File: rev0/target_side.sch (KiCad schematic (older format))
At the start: 11 parts, among them IC1 ECP5-BGA256, U9 USB3343

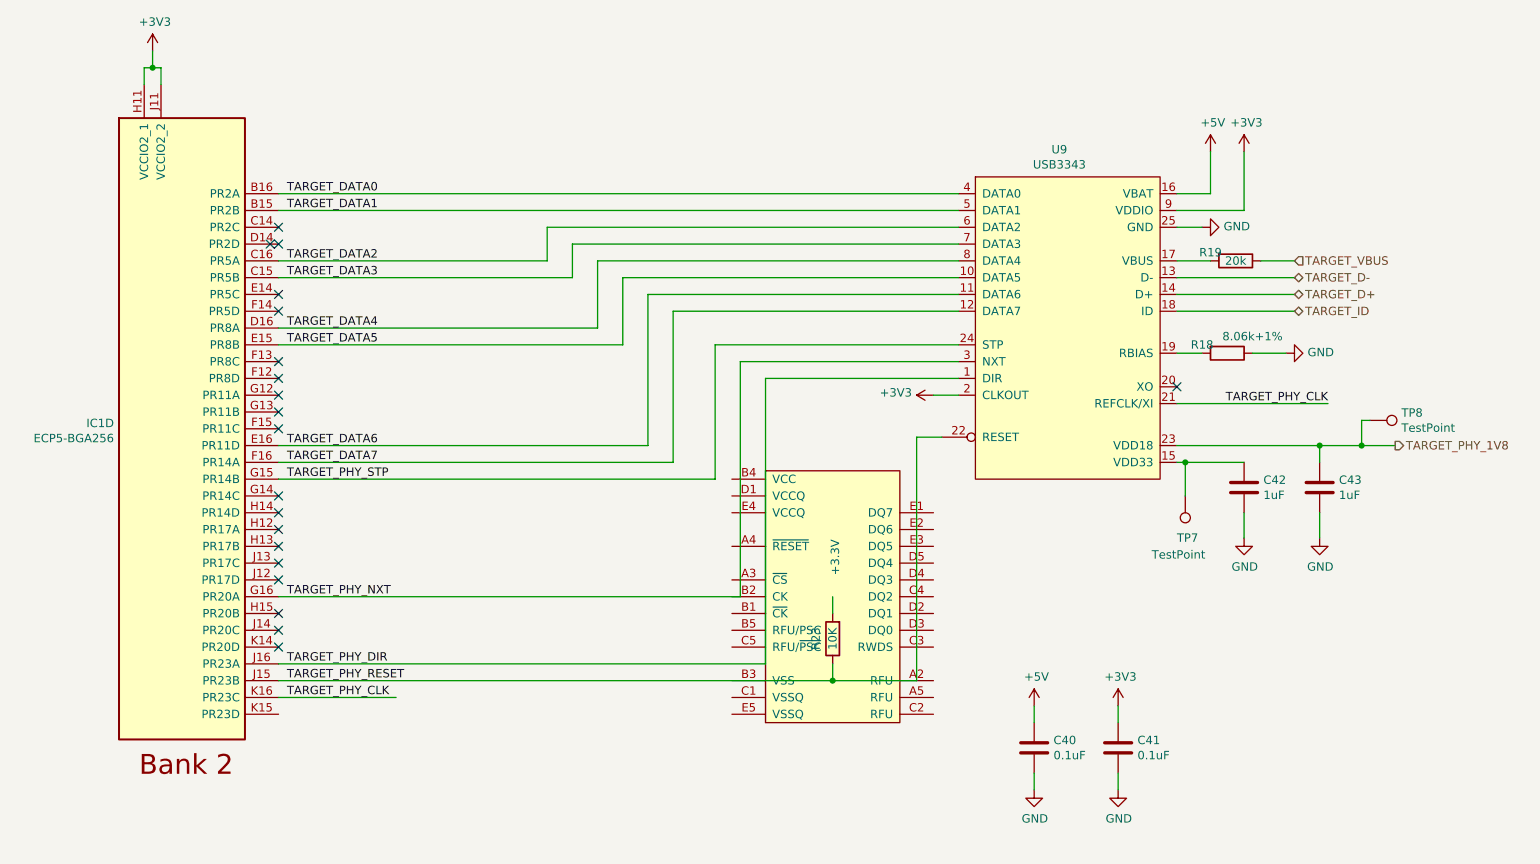
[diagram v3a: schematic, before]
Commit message: rev0: get most of the major routing done
still needs power routing, length matching for the busses,
and routing for the misc control stuff
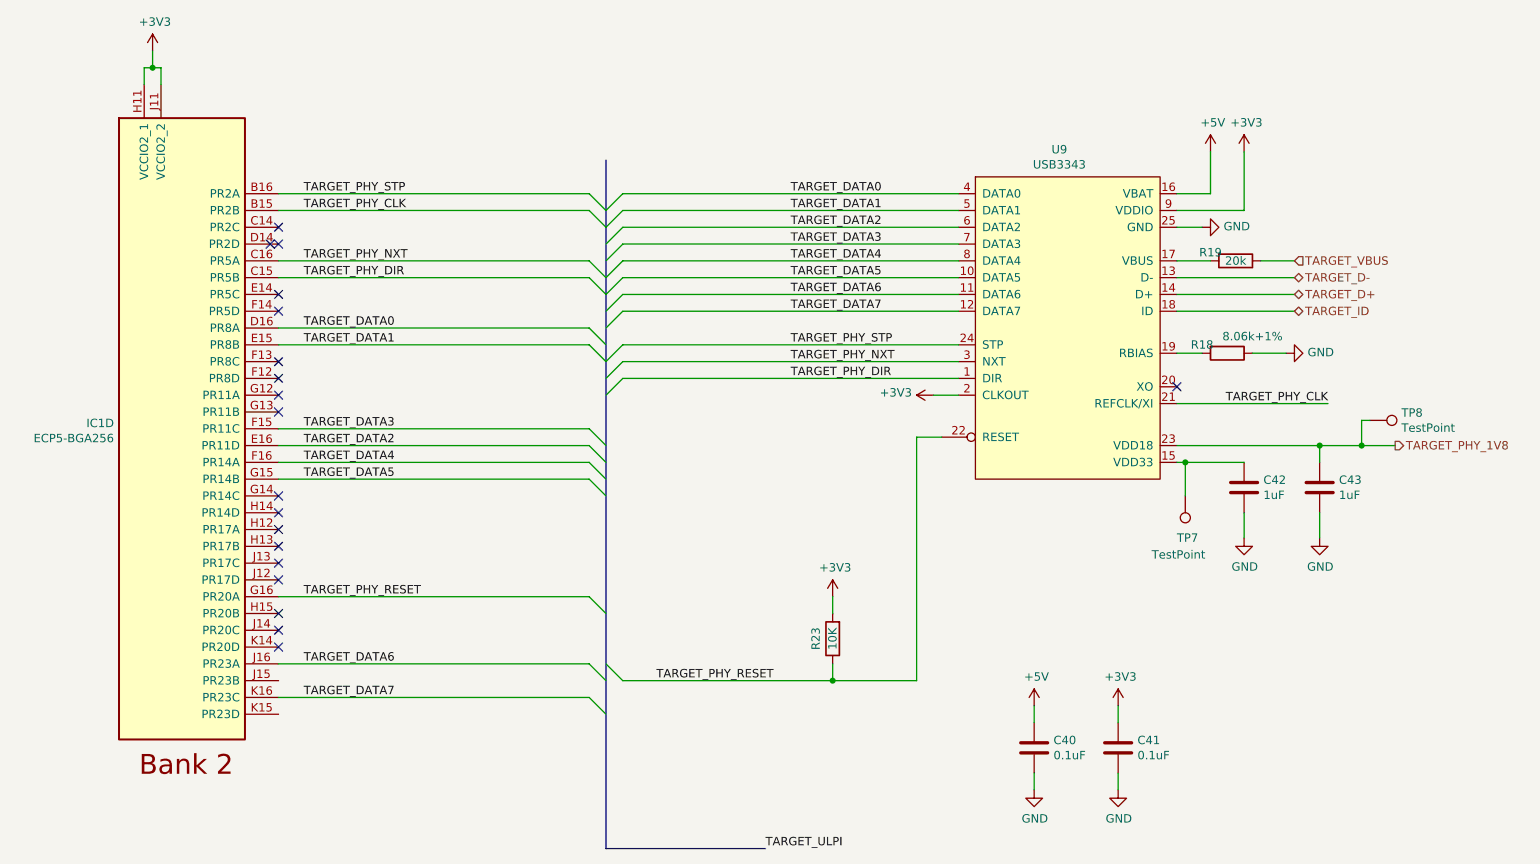
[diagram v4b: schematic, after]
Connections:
- net +3V3: now also R23.2
- net TARGET_DATA0: now also IC1.D16 (PR8A); no longer IC1.B16 (PR2A)
- net TARGET_DATA1: now also IC1.E15 (PR8B); no longer IC1.B15 (PR2B)
- net TARGET_DATA2: now also IC1.E16 (PR11D); no longer IC1.C16 (PR5A)
- net TARGET_DATA3: now also IC1.F15 (PR11C); no longer IC1.C15 (PR5B)
- net TARGET_DATA4: now also IC1.F16 (PR14A); no longer IC1.D16 (PR8A)
- net TARGET_DATA5: now also IC1.G15 (PR14B); no longer IC1.E15 (PR8B)
- net TARGET_DATA6: now also IC1.J16 (PR23A); no longer IC1.E16 (PR11D)
- net TARGET_DATA7: now also IC1.K16 (PR23C); no longer IC1.F16 (PR14A)
- net TARGET_PHY_CLK: now also IC1.B15 (PR2B); no longer IC1.K16 (PR23C)
- net TARGET_PHY_DIR: now also IC1.C15 (PR5B); no longer IC1.J16 (PR23A)
- net TARGET_PHY_NXT: now also IC1.C16 (PR5A); no longer IC1.G16 (PR20A)
- net TARGET_PHY_RESET: now also IC1.G16 (PR20A); no longer IC1.J15 (PR23B)
- net TARGET_PHY_STP: now also IC1.B16 (PR2A); no longer IC1.G15 (PR14B)
- no-connect marks 20 -> 19
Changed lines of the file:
@@
 	6650 3750 6500 3750
-Wire Wire Line
-	6650 3650 5500 3650
-Wire Wire Line
-	6650 3250 4950 3250
-Wire Wire Line
-	4650 3050 6650 3050
-Wire Wire Line
-	4800 3150 6650 3150
-Wire Wire Line
-	4500 2950 6650 2950
 Wire Wire Line
 	8450 2950 8650 2950
@@
 $EndComp
 Wire Wire Line
-	2600 2550 6650 2550
-Wire Wire Line
-	6650 2850 4350 2850
-Wire Wire Line
-	4200 2750 6650 2750
-Wire Wire Line
-	2600 2650 6650 2650
-Wire Wire Line
-	4200 2750 4200 2950
-Wire Wire Line
-	4200 2950 2600 2950
-Wire Wire Line
-	4350 2850 4350 3050
-Wire Wire Line
-	4350 3050 2600 3050
-Wire Wire Line
-	4500 2950 4500 3350
-Wire Wire Line
-	4500 3350 2600 3350
-Wire Wire Line
-	2600 3450 4650 3450
-Wire Wire Line
-	4650 3450 4650 3050
-Wire Wire Line
-	4800 3150 4800 4050
-Wire Wire Line
-	4800 4050 2600 4050
-Wire Wire Line
-	4950 3250 4950 4150
-Wire Wire Line
-	4950 4150 2600 4150
-Wire Wire Line
-	5200 3450 5200 4250
-Wire Wire Line
-	5200 3450 6650 3450
-Wire Wire Line
-	5200 4250 2600 4250
-Wire Wire Line
-	5350 3550 5350 4950
-Wire Wire Line
-	5350 4950 2600 4950
-Wire Wire Line
-	5350 3550 6650 3550
-Wire Wire Line
-	5500 3650 5500 5350
-Wire Wire Line
-	5500 5350 2600 5350
-Wire Wire Line
 	6400 4000 6400 5450
-Text Label 2650 5550 0    50   ~ 0
+Text Label 2750 2650 0    50   ~ 0
 TARGET_PHY_CLK
-Wire Wire Line
-	3300 5550 2600 5550
-Text Label 2650 5450 0    50   ~ 0
-TARGET_PHY_RESET
-Text Label 2650 5350 0    50   ~ 0
+Text Label 5650 3650 0    50   ~ 0
 TARGET_PHY_DIR
-Text Label 2650 4250 0    50   ~ 0
+Text Label 5650 3450 0    50   ~ 0
 TARGET_PHY_STP
-Text Label 2650 4950 0    50   ~ 0
+Text Label 5650 3550 0    50   ~ 0
 TARGET_PHY_NXT
-Text Label 2650 4150 0    50   ~ 0
+Text Label 5650 3250 0    50   ~ 0
 TARGET_DATA7
-Text Label 2650 4050 0    50   ~ 0
+Text Label 5650 3150 0    50   ~ 0
 TARGET_DATA6
-Text Label 2650 3450 0    50   ~ 0
+Text Label 5650 3050 0    50   ~ 0
 TARGET_DATA5
-Text Label 2650 3350 0    50   ~ 0
+Text Label 5650 2950 0    50   ~ 0
 TARGET_DATA4
-Text Label 2650 3050 0    50   ~ 0
+Text Label 5650 2850 0    50   ~ 0
 TARGET_DATA3
-Text Label 2650 2950 0    50   ~ 0
+Text Label 5650 2750 0    50   ~ 0
 TARGET_DATA2
-Text Label 2650 2650 0    50   ~ 0
+Text Label 5650 2650 0    50   ~ 0
 TARGET_DATA1
-Text Label 2650 2550 0    50   ~ 0
+Text Label 5650 2550 0    50   ~ 0
 TARGET_DATA0
 NoConn ~ 2600 2750
@@
 NoConn ~ 2600 3750
 NoConn ~ 2600 3850
-NoConn ~ 2600 3950
 NoConn ~ 2600 4350
 NoConn ~ 2600 4450
@@
 Wire Wire Line
 	5900 5050 5900 4950
-$Comp
-L support_hardware:S27KS0641 #PWR?
-U 1 1 5E15EF17
+Wire Wire Line
+	5900 5450 6400 5450
+NoConn ~ 7950 3700
+$Comp
+L power:+3V3 #PWR0109
+U 1 1 5DFA29A4
 P 5900 4950
-AR Path="/5DD754D4/5E15EF17" Ref="#PWR?"  Part="1"
-AR Path="/5DDDB747/5E15EF17" Ref="#PWR0100"  Part="1"
-AR Path="/5E15EF17" Ref="#PWR0100"  Part="1"
-F 0 "#PWR0100" H 5900 4800 50  0001 C CNN
-F 1 "+3.3V" V 5915 5078 50  0000 L CNN
+F 0 "#PWR0109" H 5900 4800 50  0001 C CNN
+F 1 "+3V3" H 5915 5123 50  0000 C CNN
 F 2 "" H 5900 4950 50  0001 C CNN
 F 3 "" H 5900 4950 50  0001 C CNN
@@
 	1    0    0    -1
 $EndComp
-Wire Wire Line
-	2600 5450 5900 5450
+Wire Bus Line
+	4550 6450 5500 6450
+Wire Wire Line
+	2600 2550 4450 2550
+Wire Wire Line
+	2600 2650 4450 2650
+Entry Wire Line
+	4450 2550 4550 2650
+Entry Wire Line
+	4450 2650 4550 2750
+Wire Wire Line
+	2600 2950 4450 2950
+Wire Wire Line
+	2600 3050 4450 3050
+Wire Wire Line
+	2600 3350 4450 3350
+Wire Wire Line
+	2600 3450 4450 3450
+Wire Wire Line
+	2600 4050 4450 4050
+Wire Wire Line
+	2600 4150 4450 4150
+Wire Wire Line
+	2600 4250 4450 4250
+Wire Wire Line
+	2600 5350 4450 5350
+Wire Wire Line
+	6650 3450 4650 3450
+Wire Wire Line
+	6650 3550 4650 3550
+Wire Wire Line
+	6650 3650 4650 3650
+Wire Wire Line
+	2600 5550 4450 5550
+Entry Wire Line
+	4550 3550 4650 3450
+Entry Wire Line
+	4550 3650 4650 3550
+Entry Wire Line
+	4550 3750 4650 3650
+Entry Wire Line
+	4550 3350 4650 3250
+Entry Wire Line
+	4550 3250 4650 3150
+Entry Wire Line
+	4550 3150 4650 3050
+Entry Wire Line
+	4550 3050 4650 2950
+Entry Wire Line
+	4550 2950 4650 2850
+Entry Wire Line
+	4550 2850 4650 2750
+Entry Wire Line
+	4550 2650 4650 2550
+Entry Wire Line
+	4550 2750 4650 2650
+Wire Wire Line
+	6650 3250 4650 3250
+Wire Wire Line
+	6650 3150 4650 3150
+Wire Wire Line
+	6650 3050 4650 3050
+Wire Wire Line
+	6650 2950 4650 2950
+Wire Wire Line
+	6650 2850 4650 2850
+Wire Wire Line
+	6650 2750 4650 2750
+Wire Wire Line
+	4650 2650 6650 2650
+Wire Wire Line
+	6650 2550 4650 2550
+Text Label 5500 6450 0    50   ~ 0
+TARGET_ULPI
+Text Label 2750 2550 0    50   ~ 0
+TARGET_PHY_STP
+Text Label 2750 3050 0    50   ~ 0
+TARGET_PHY_DIR
+Text Label 2750 2950 0    50   ~ 0
+TARGET_PHY_NXT
+Text Label 2750 3350 0    50   ~ 0
+TARGET_DATA0
+Text Label 2750 3450 0    50   ~ 0
+TARGET_DATA1
+Text Label 2750 4050 0    50   ~ 0
+TARGET_DATA2
+Wire Wire Line
+	2600 3950 4450 3950
+Text Label 2750 3950 0    50   ~ 0
+TARGET_DATA3
+Text Label 2750 4150 0    50   ~ 0
+TARGET_DATA4
+Text Label 2750 4950 0    50   ~ 0
+TARGET_PHY_RESET
+Text Label 2750 4250 0    50   ~ 0
+TARGET_DATA5
+Text Label 2750 5350 0    50   ~ 0
+TARGET_DATA6
+Text Label 2750 5550 0    50   ~ 0
+TARGET_DATA7
+Entry Wire Line
+	4450 2950 4550 3050
+Entry Wire Line
+	4450 3050 4550 3150
+Entry Wire Line
+	4450 3350 4550 3450
+Entry Wire Line
+	4450 3450 4550 3550
+Entry Wire Line
+	4450 3950 4550 4050
+Entry Wire Line
+	4450 4050 4550 4150
+Entry Wire Line
+	4450 4150 4550 4250
+Entry Wire Line
+	4450 4250 4550 4350
+Entry Wire Line
+	4450 4950 4550 5050
+Entry Wire Line
+	4450 5350 4550 5450
+Entry Wire Line
+	4450 5550 4550 5650
+Wire Wire Line
+	2600 4950 4450 4950
+Wire Wire Line
+	5900 5450 4650 5450
+Wire Bus Line
+	4550 2350 4550 6450
 Connection ~ 5900 5450
-Wire Wire Line
-	5900 5450 6400 5450
-NoConn ~ 7950 3700
+Entry Wire Line
+	4550 5350 4650 5450
+Text Label 4850 5450 0    50   ~ 0
+TARGET_PHY_RESET
 $EndSCHEMATC

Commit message: rev0: routing: get our routing significnatly more complete :)
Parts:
- removed TP7, TP8: TestPoint, TestPoint:TestPoint_Pad_1.0x1.0mm, symbol Connector:TestPoint
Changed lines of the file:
@@
 AR Path="/5DD754D4/5DDE2B06" Ref="R?"  Part="1"
 AR Path="/5DDDB747/5DDE2B06" Ref="R18"  Part="1"
-F 0 "R18" V 8200 3350 50  0000 C CNN
+F 0 "R18" V 8200 3300 50  0000 C CNN
 F 1 "8.06k+1%" V 8150 3650 50  0000 C CNN
 F 2 "Resistor_SMD:R_0402_1005Metric" V 8180 3500 50  0001 C CNN
@@
 Text HLabel 8650 2950 2    50   Input ~ 0
 TARGET_VBUS
-Wire Wire Line
-	8000 4150 8350 4150
-Connection ~ 8000 4150
-Wire Wire Line
-	8000 4350 8000 4150
-$Comp
-L Connector:TestPoint TP?
-U 1 1 5DDE2B2D
-P 8000 4350
-AR Path="/5DCD9772/5DDE2B2D" Ref="TP?"  Part="1"
-AR Path="/5DD754D4/5DDE2B2D" Ref="TP?"  Part="1"
-AR Path="/5DDDB747/5DDE2B2D" Ref="TP7"  Part="1"
-F 0 "TP7" H 8050 4600 50  0000 R CNN
-F 1 "TestPoint" H 8200 4700 50  0000 R CNN
-F 2 "TestPoint:TestPoint_Pad_1.0x1.0mm" H 8200 4350 50  0001 C CNN
-F 3 "~" H 8200 4350 50  0001 C CNN
-	1    8000 4350
-	-1   0    0    1
-$EndComp
-Wire Wire Line
-	9050 4050 9250 4050
-Connection ~ 9050 4050
-Wire Wire Line
-	9050 3900 9050 4050
-Wire Wire Line
-	9100 3900 9050 3900
-$Comp
-L Connector:TestPoint TP?
-U 1 1 5DDE2B37
-P 9100 3900
-AR Path="/5DCD9772/5DDE2B37" Ref="TP?"  Part="1"
-AR Path="/5DD754D4/5DDE2B37" Ref="TP?"  Part="1"
-AR Path="/5DDDB747/5DDE2B37" Ref="TP8"  Part="1"
-F 0 "TP8" V 9055 4087 50  0000 L CNN
-F 1 "TestPoint" V 9145 4087 50  0000 L CNN
-F 2 "TestPoint:TestPoint_Pad_1.0x1.0mm" H 9300 3900 50  0001 C CNN
-F 3 "~" H 9300 3900 50  0001 C CNN
-	1    9100 3900
-	0    1    1    0
-$EndComp
-Wire Wire Line
-	8800 4050 9050 4050
 Connection ~ 8800 4050
 Wire Wire Line
@@
 	1    0    0    -1
 $EndComp
-Wire Wire Line
-	7950 4150 8000 4150
 Wire Wire Line
 	8350 4600 8350 4450
@@
 Wire Wire Line
 	5900 5450 4650 5450
-Wire Bus Line
-	4550 2350 4550 6450
 Connection ~ 5900 5450
 Entry Wire Line
@@
 Text Label 4850 5450 0    50   ~ 0
 TARGET_PHY_RESET
+Wire Wire Line
+	8800 4050 9250 4050
+Wire Wire Line
+	7950 4150 8350 4150
+Wire Bus Line
+	4550 2350 4550 6450
 $EndSCHEMATC

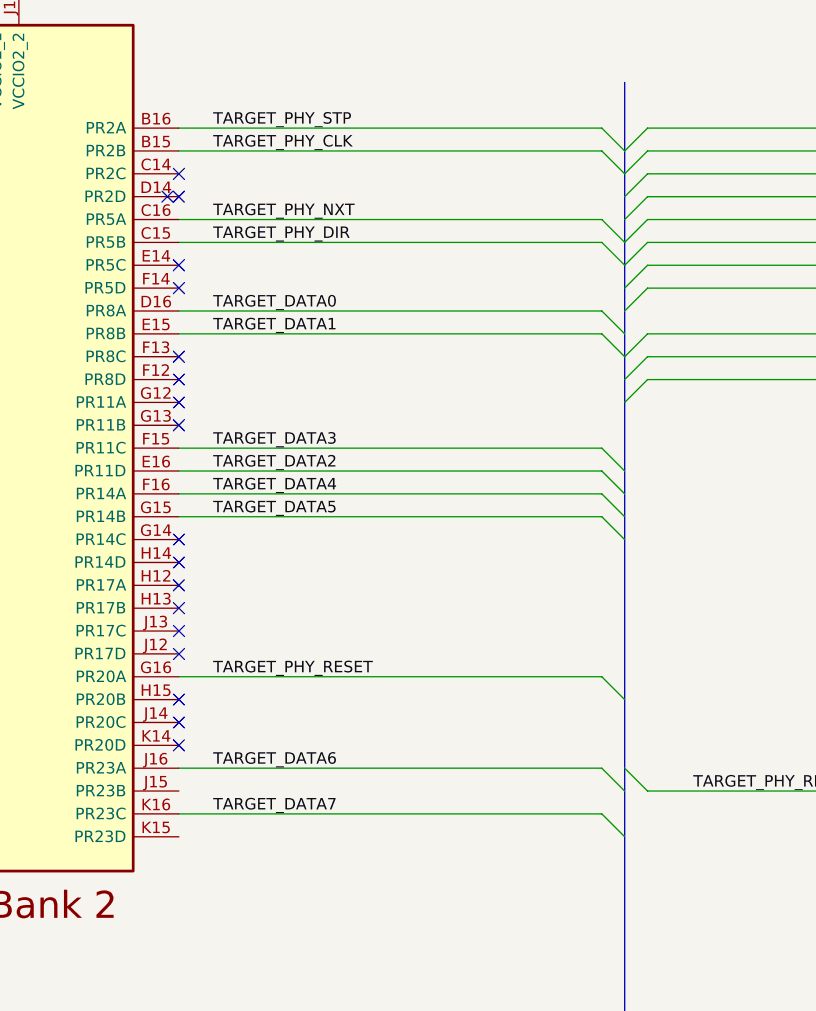
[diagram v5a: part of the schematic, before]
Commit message: rev0: implement all of the routing except length matching
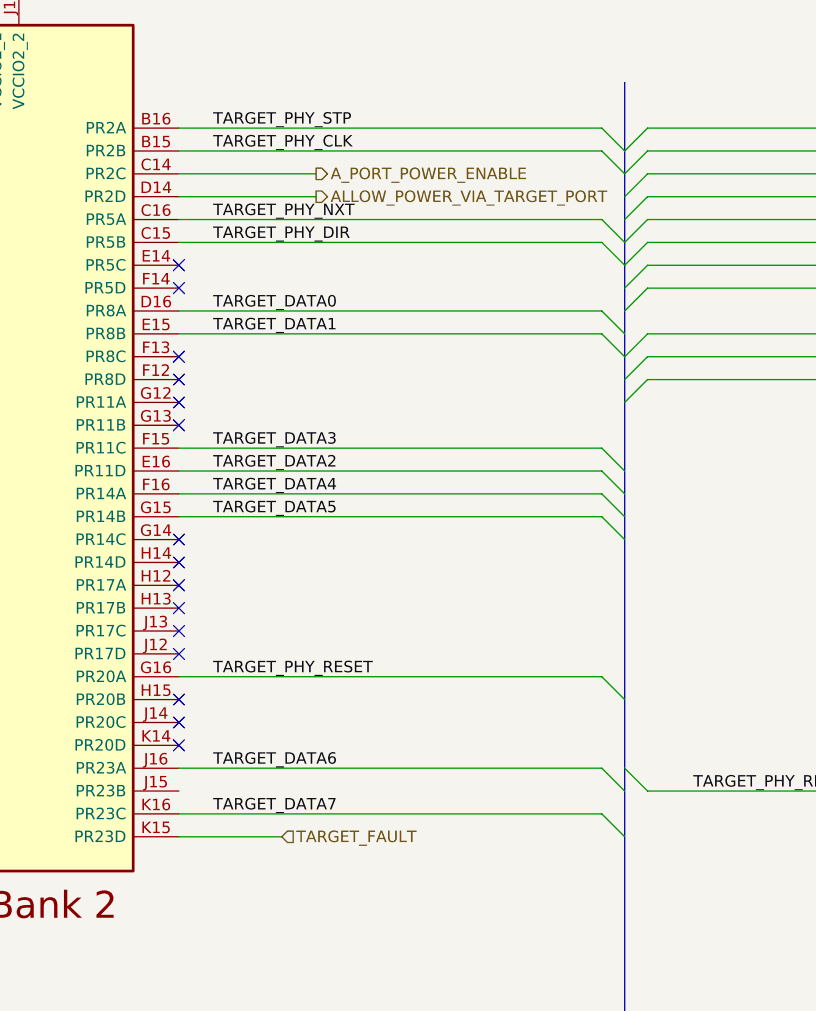
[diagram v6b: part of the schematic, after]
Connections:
- net A_PORT_POWER_ENABLE: now reaches IC1.C14 (PR2C)
- net ALLOW_POWER_VIA_TARGET_PORT: now reaches IC1.D14 (PR2D)
- net TARGET_FAULT: now reaches IC1.K15 (PR23D)
- no-connect marks 19 -> 16
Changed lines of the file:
@@
 Text Label 5650 2550 0    50   ~ 0
 TARGET_DATA0
-NoConn ~ 2600 2750
-NoConn ~ 2550 2850
-NoConn ~ 2600 2850
 NoConn ~ 2600 3550
 NoConn ~ 2600 3150
@@
 Wire Wire Line
 	7950 4150 8350 4150
+Wire Wire Line
+	2600 5650 3050 5650
+Text HLabel 3050 5650 2    50   Input ~ 0
+TARGET_FAULT
+Text HLabel 3200 2750 2    50   Output ~ 0
+A_PORT_POWER_ENABLE
+Wire Wire Line
+	2600 2750 3200 2750
+Text HLabel 3200 2850 2    50   Output ~ 0
+ALLOW_POWER_VIA_TARGET_PORT
+Wire Wire Line
+	3200 2850 2600 2850
 Wire Bus Line
 	4550 2350 4550 6450
